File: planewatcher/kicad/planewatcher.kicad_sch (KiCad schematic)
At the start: 14 parts, among them J2 RF_IN, J3 BMI-S-209-F, J4 FPGA BANK 33, J5 FPGA BANK 35 V1.2/V1.3, J6 GPS _IN

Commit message: update BoM to available parts from LCSC
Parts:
- C1: MPN GCJ31CR71A226KE01K -> CL31B226KPHNNNE; Manufacturer Murata Electronics -> Samsung Electro-Mechanics; lcsc_id C3883047 -> C87996
- C3: MPN GRM1555C1H102FA01D -> GCM1555C1H102FA16D; lcsc_id C161523 -> C126493
- L1: MPN 74269262601 -> MPZ1608S601ATA00; Manufacturer Würth Elektronik -> TDK; Package 0805 -> 0603; lcsc_id C5914022 -> C107335
- R1: MPN RT0402FRE1310KL -> ERA-2AEB103X; Manufacturer YAGEO -> Panasonic Industry; lcsc_id C5455557 -> C191915
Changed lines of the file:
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@@
 			)
 		)
-		(property "MPN" "GCJ31CR71A226KE01K"
+		(property "MPN" "CL31B226KPHNNNE"
 			(at 120.65 38.1 0)
 			(hide yes)
@@
 			)
 		)
-		(property "Manufacturer" "Murata Electronics"
+		(property "Manufacturer" "Samsung Electro-Mechanics"
 			(at 120.65 38.1 0)
 			(hide yes)
@@
 			)
 		)
-		(property "lcsc_id" "C3883047"
+		(property "lcsc_id" "C87996"
 			(at 120.65 38.1 0)
 			(hide yes)
@@
 			)
 		)
-		(property "Description" "10 kOhms ±1% 0.063W, 1/16W Chip Resistor 0402 (1005 Metric) Moisture Resistant Thin Film"
+		(property "Description" "10 kOhms ±0.1% 0.063W, 1/16W Chip Resistor 0402 (1005 Metric) Automotive AEC-Q200 Thin Film"
 			(at 184.15 29.21 0)
 			(hide yes)
@@
 			)
 		)
-		(property "MPN" "RT0402FRE1310KL"
+		(property "MPN" "ERA-2AEB103X"
 			(at 184.15 29.21 0)
 			(hide yes)
@@
 			)
 		)
-		(property "Manufacturer" "YAGEO"
+		(property "Manufacturer" "Panasonic Industry"
 			(at 184.15 29.21 0)
 			(hide yes)
@@
 			)
 		)
-		(property "lcsc_id" "C5455557"
+		(property "lcsc_id" "C191915"
 			(at 184.15 29.21 0)
 			(hide yes)
@@
 			)
 		)
-		(property "MPN" "GRM1555C1H102FA01D"
+		(property "MPN" "GCM1555C1H102FA16D"
 			(at 146.05 38.1 0)
 			(hide yes)
@@
 			)
 		)
-		(property "lcsc_id" "C161523"
+		(property "lcsc_id" "C126493"
 			(at 146.05 38.1 0)
 			(hide yes)
@@
 			)
 		)
-		(property "Package" "0805"
+		(property "Package" "0603"
 			(at 109.22 34.29 0)
 			(hide yes)
@@
 			)
 		)
-		(property "MPN" "74269262601"
+		(property "MPN" "MPZ1608S601ATA00"
 			(at 109.22 34.29 0)
 			(hide yes)
@@
 			)
 		)
-		(property "Manufacturer" "Würth Elektronik"
+		(property "Manufacturer" "TDK"
 			(at 109.22 34.29 0)
 			(hide yes)
@@
 			)
 		)
-		(property "lcsc_id" "C5914022"
+		(property "lcsc_id" "C107335"
 			(at 109.22 34.29 0)
 			(hide yes)

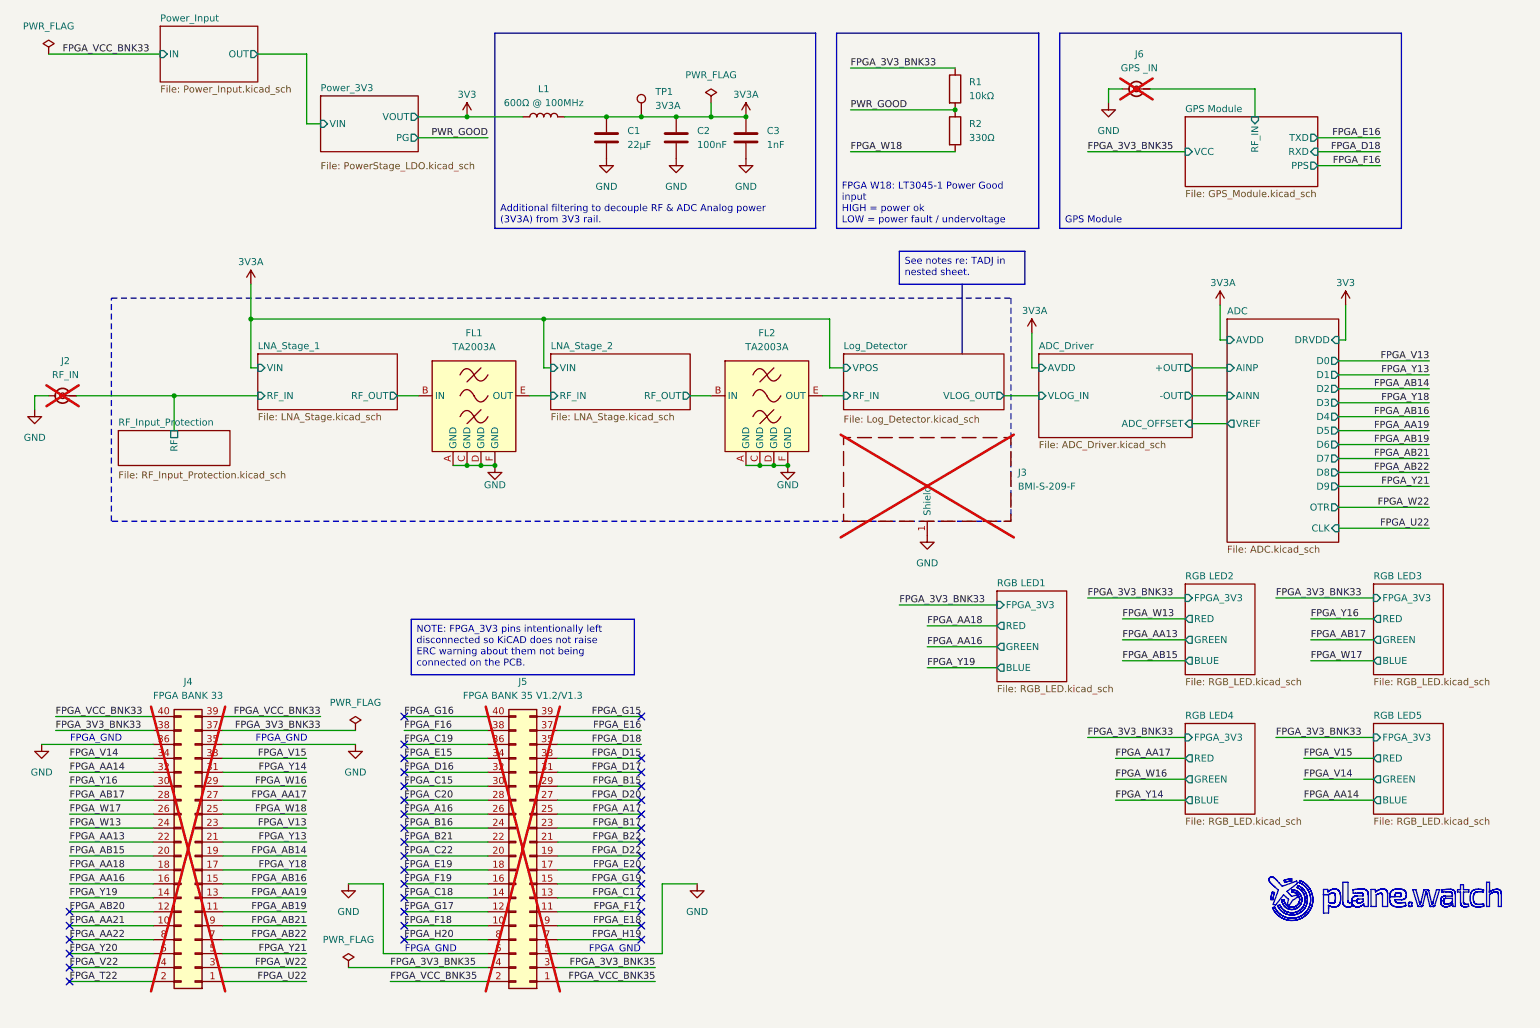
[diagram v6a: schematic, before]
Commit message: add pink led for gps pps + attach gps reset to fpga
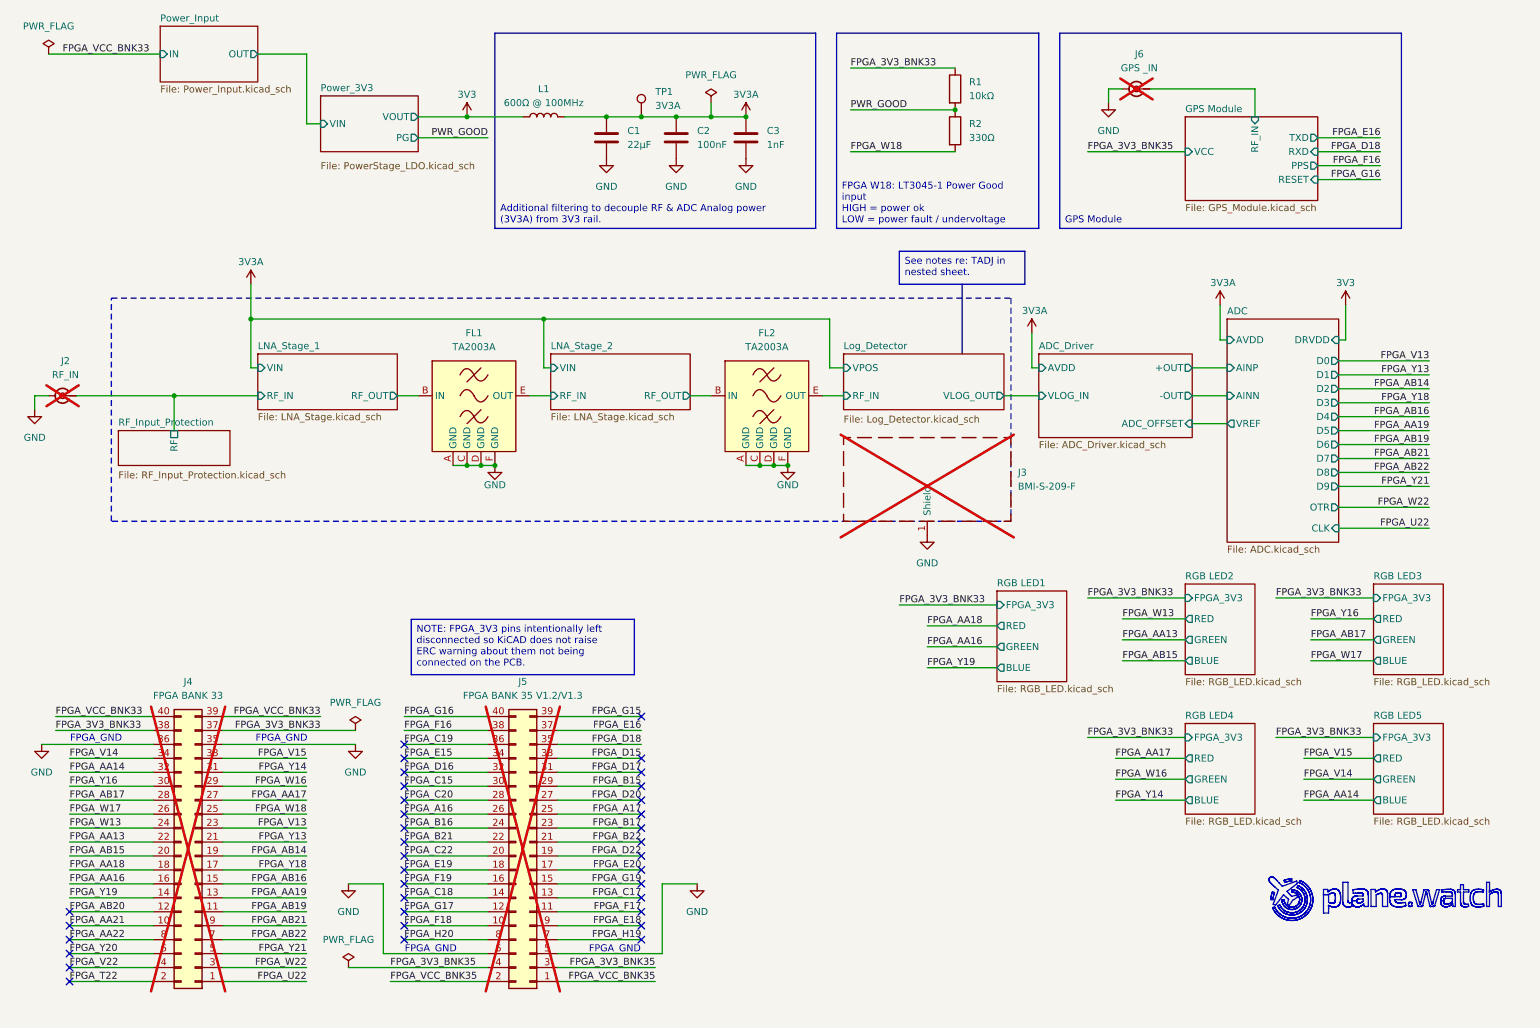
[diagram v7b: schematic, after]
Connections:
- no-connect marks 37 -> 36
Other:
- sheet GPS Module ports: added RESET; removed none
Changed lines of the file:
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@@
 	)
 	(no_connect
-		(at 83.82 143.51)
-	)
-	(no_connect
 		(at 127 161.29)
 	)
@@
 	(wire
 		(pts
+			(xy 250.19 45.72) (xy 261.62 45.72)
+		)
+		(stroke
+			(width 0)
+			(type default)
+		)
+	)
+	(wire
+		(pts
 			(xy 130.81 173.99) (xy 137.16 173.99)
 		)
@@
 		)
 	)
+	(label "FPGA_G16"
+		(at 261.62 45.72 180)
+		(effects
+			(font
+				(size 1.27 1.27)
+			)
+			(justify right bottom)
+		)
+	)
 	(label "FPGA_H19"
 		(at 127 184.15 180)
@@
 	(sheet
 		(at 226.06 34.29)
-		(size 24.13 12.7)
+		(size 24.13 15.24)
 		(exclude_from_sim no)
 		(in_bom yes)
@@
 		)
 		(property "Sheetfile" "GPS_Module.kicad_sch"
-			(at 226.06 47.5746 0)
+			(at 226.06 50.1146 0)
 			(show_name no)
 			(do_not_autoplace no)
@@
 			(effects
 				(font
+					(size 1.27 1.27)
+				)
+				(justify right)
+			)
+		)
+		(pin "RESET" input
+			(at 250.19 45.72 0)
+			(effects
+				(font

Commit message: Add bias-tee power switch & connect GPS TP2
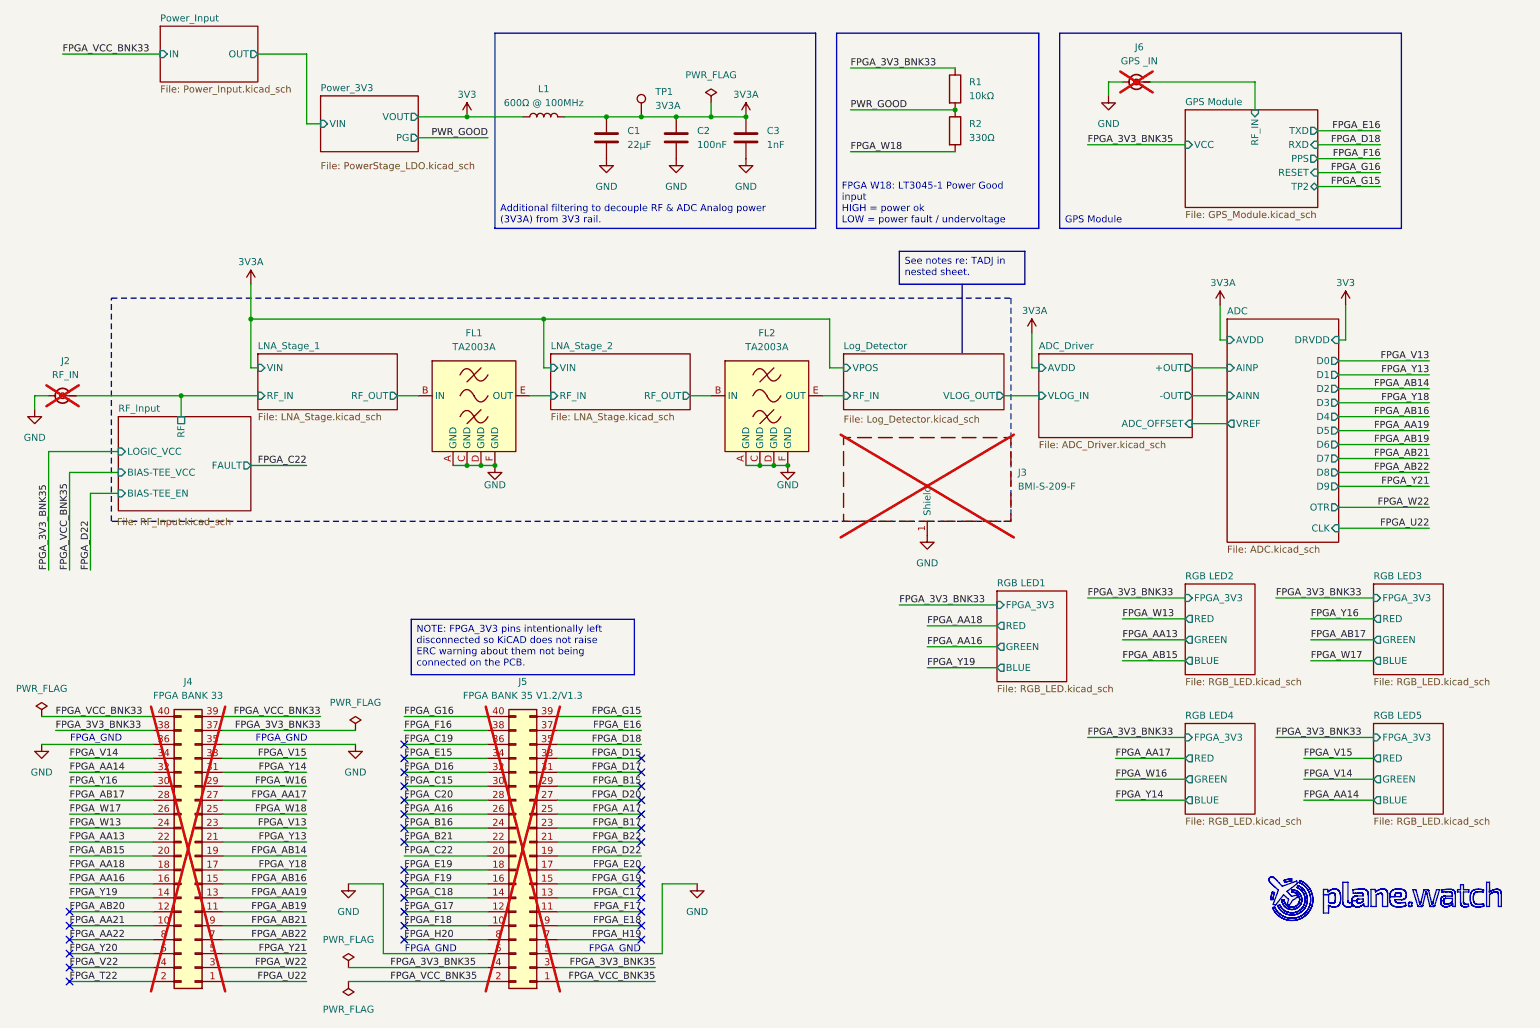
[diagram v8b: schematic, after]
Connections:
- no-connect marks 36 -> 33
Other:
- sheet RF_Input_Protection renamed RF_Input
- sheet GPS Module ports: added TP2; removed none
- sheet RF_Input: file RF_Input_Protection.kicad_sch -> RF_Input.kicad_sch
- sheet RF_Input ports: added BIAS-TEE_EN, BIAS-TEE_VCC, FAULT, LOGIC_VCC; removed none
- moved on the sheet: J6
